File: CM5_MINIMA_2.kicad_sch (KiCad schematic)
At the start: 15 parts, among them J101 USB_C_Receptacle_USB2.0

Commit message: power symbols
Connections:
- net +3V3 renamed +3V3_PI
- no-connect marks 6 -> 7
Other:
- sheet CM5 ports: added none; removed GPIO5, GPIO6, GPIO7
- sheet DSI_CSI ports: added none; removed 3V3
- sheet Ethernet ports: added none; removed 3V3
- sheet HDMI ports: added none; removed 5V
- sheet IO ports: added nLED_ACTIVITY; removed 3V3, 5V, nACTIVITY_LED
- sheet PCIe-M2 ports: added none; removed +5v
- sheet USB ports: added none; removed 5V
- moved on the sheet: C101, C102, TP101

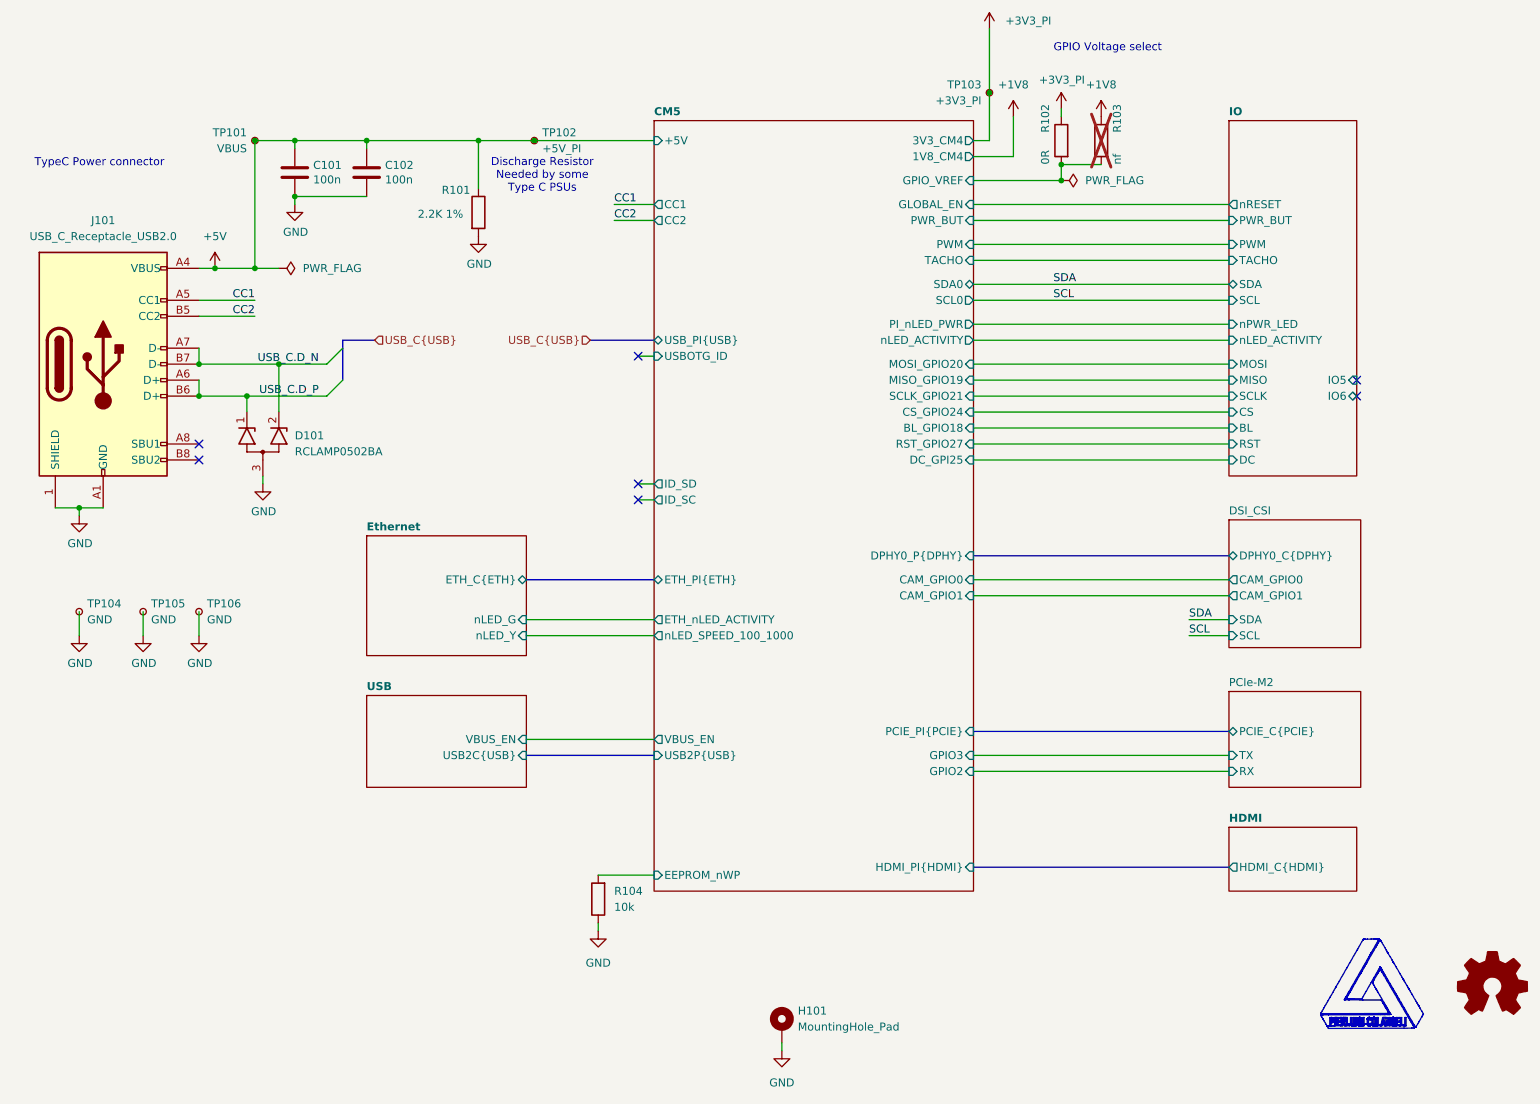
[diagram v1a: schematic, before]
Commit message: changed i2c connector and nrpiboot
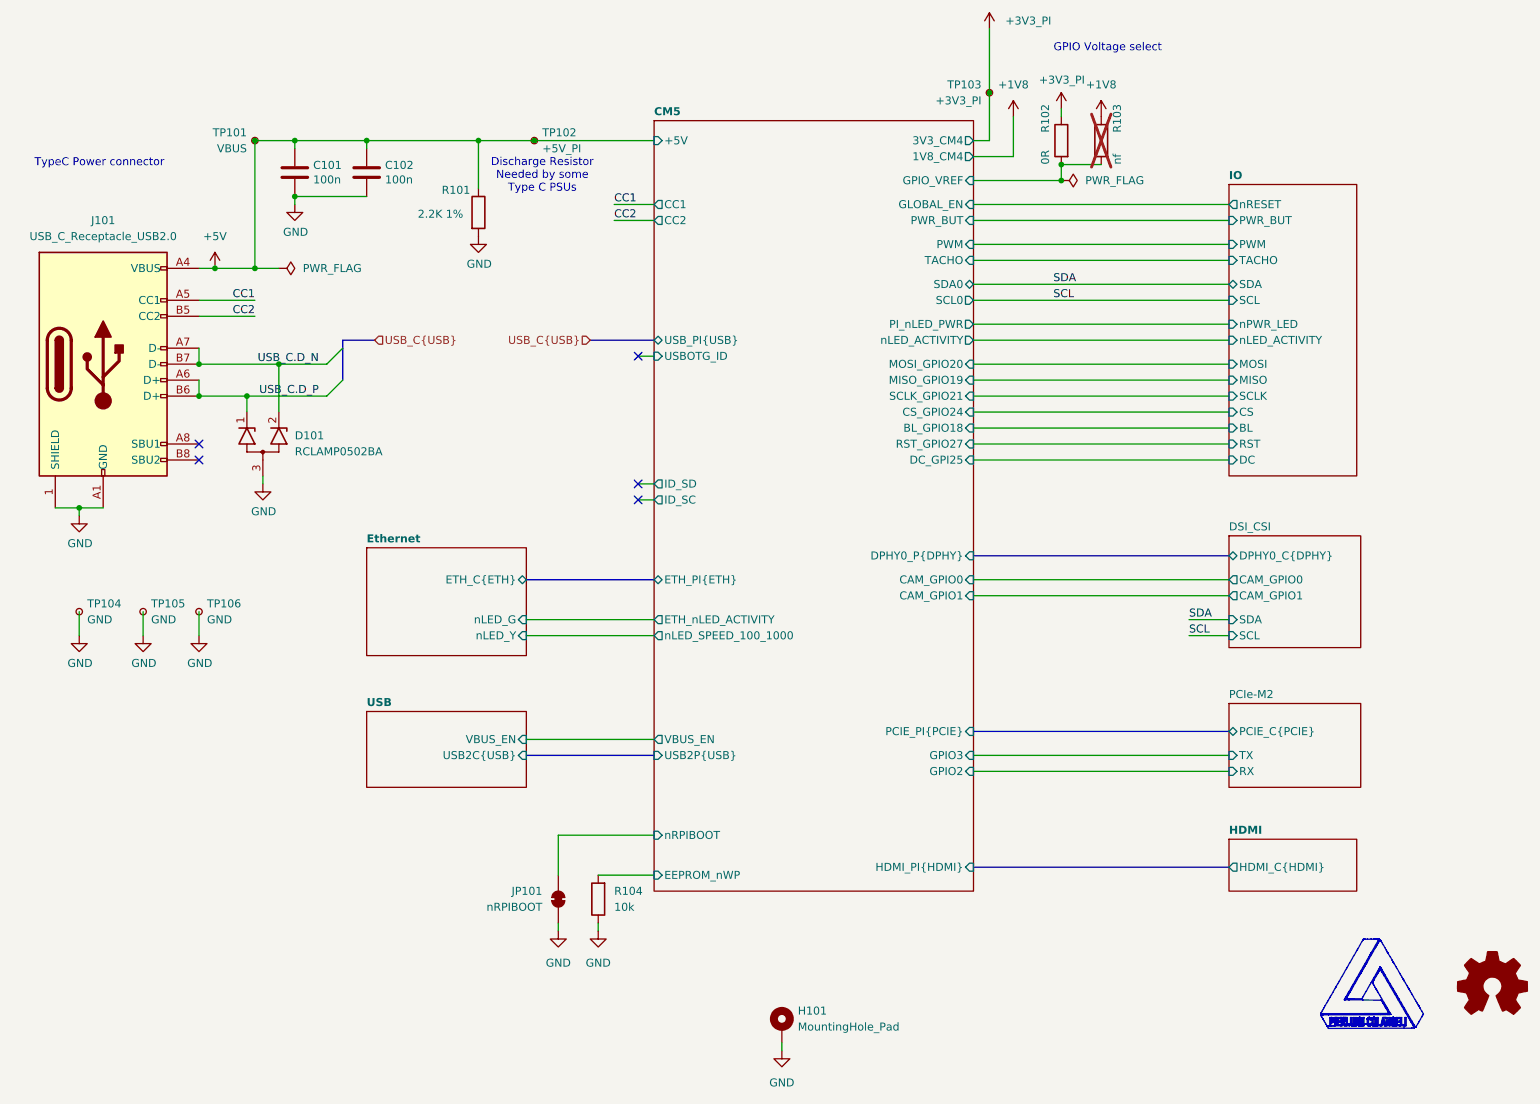
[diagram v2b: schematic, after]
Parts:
- added JP101: nRPIBOOT, Jumper:SolderJumper-2_P1.3mm_Bridged_RoundedPad1.0x1.5mm, symbol Jumper:SolderJumper_2_Bridged
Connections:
- net GND: now also JP101.1 (A)
- new net CM5/nRPIBOOT: JP101.2 (B)
- no-connect marks 7 -> 5
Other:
- sheet CM5 ports: added nRPIBOOT; removed none
- sheet IO ports: added none; removed IO5, IO6
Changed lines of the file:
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@@
 	)
 	(no_connect
-		(at 234.95 80.01)
-	)
-	(no_connect
 		(at 120.65 73.66)
 	)
@@
 		(at 120.65 96.52)
 	)
-	(no_connect
-		(at 234.95 77.47)
-	)
 	(bus_entry
 		(at 71.12 74.93)
@@
 	(wire
 		(pts
+			(xy 107.95 163.83) (xy 107.95 165.1)
+		)
+		(stroke
+			(width 0)
+			(type default)
+		)
+	)
+	(wire
+		(pts
 			(xy 31.75 114.3) (xy 31.75 118.11)
 		)
@@
 		)
 	)
+	(wire
+		(pts
+			(xy 107.95 149.86) (xy 123.19 149.86)
+		)
+		(stroke
+			(width 0)
+			(type default)
+		)
+	)
 	(bus
 		(pts
@@
 	(wire
 		(pts
+			(xy 107.95 149.86) (xy 107.95 156.21)
+		)
+		(stroke
+			(width 0)
+			(type default)
+		)
+	)
+	(wire
+		(pts
 			(xy 77.47 39.37) (xy 95.25 39.37)
 		)
@@
 		)
 	)
+	(symbol
+		(lib_id "Jumper:SolderJumper_2_Bridged")
+		(at 107.95 160.02 270)
+		(mirror x)
+		(unit 1)
+		(exclude_from_sim yes)
+		(in_bom no)
+		(on_board yes)
+		(dnp no)
+		(property "Reference" "JP101"
+			(at 105.41 158.7499 90)
+			(effects
+				(font
+					(size 1.27 1.27)
+				)
+				(justify right)
+			)
+		)
+		(property "Value" "nRPIBOOT"
+			(at 105.41 161.2899 90)
+			(effects
+				(font
+					(size 1.27 1.27)
+				)
+				(justify right)
+			)
+		)
+		(property "Footprint" "Jumper:SolderJumper-2_P1.3mm_Bridged_RoundedPad1.0x1.5mm"
+			(at 107.95 160.02 0)
+			(effects
+				(font
+					(size 1.27 1.27)
+				)
+				(hide yes)
+			)
+		)
+		(property "Datasheet" "~"
+			(at 107.95 160.02 0)
+			(effects
+				(font
+					(size 1.27 1.27)
+				)
+				(hide yes)
+			)
+		)
+		(property "Description" "Solder Jumper, 2-pole, closed/bridged"
+			(at 107.95 160.02 0)
+			(effects
+				(font
+					(size 1.27 1.27)
+				)
+				(hide yes)
+			)
+		)
+		(pin "1"
+		)
+		(pin "2"
+		)
+		(instances
+			(project ""
+				(path "/b33e81d6-18a9-4b9d-a239-76a7c253462f"
+					(reference "JP101")
+					(unit 1)
+				)
+			)
+		)
+	)
+	(symbol
+		(lib_id "power:GND")
+		(at 107.95 165.1 0)
+		(unit 1)
+		(exclude_from_sim no)
+		(in_bom yes)
+		(on_board yes)
+		(dnp no)
+		(fields_autoplaced yes)
+		(property "Reference" "#PWR0105"
+			(at 107.95 171.45 0)
+			(effects
+				(font
+					(size 1.27 1.27)
+				)
+				(hide yes)
+			)
+		)
+		(property "Value" "GND"
+			(at 107.95 170.18 0)
+			(effects
+				(font
+					(size 1.27 1.27)
+				)
+			)
+		)
+		(property "Footprint" ""
+			(at 107.95 165.1 0)
+			(effects
+				(font
+					(size 1.27 1.27)
+				)
+				(hide yes)
+			)
+		)
+		(property "Datasheet" ""
+			(at 107.95 165.1 0)
+			(effects
+				(font
+					(size 1.27 1.27)
+				)
+				(hide yes)
+			)
+		)
+		(property "Description" ""
+			(at 107.95 165.1 0)
+			(effects
+				(font
+					(size 1.27 1.27)
+				)
+				(hide yes)
+			)
+		)
+		(pin "1"
+		)
+		(instances
+			(project "CM5_MINIMA_2"
+				(path "/b33e81d6-18a9-4b9d-a239-76a7c253462f"
+					(reference "#PWR0105")
+					(unit 1)
+				)
+			)
+		)
+	)
 	(sheet
-		(at 77.47 127.635)
-		(size 25.4 14.605)
+		(at 77.47 130.175)
+		(size 25.4 12.065)
 		(fields_autoplaced yes)
 		(stroke
@@
 		)
 		(property "Sheetname" "USB"
-			(at 77.47 126.9234 0)
+			(at 77.47 129.4634 0)
 			(effects
 				(font
@@
 	)
 	(sheet
-		(at 214.63 148.59)
-		(size 20.32 10.16)
+		(at 214.63 150.495)
+		(size 20.32 8.255)
 		(fields_autoplaced yes)
 		(stroke
@@
 		)
 		(property "Sheetname" "HDMI"
-			(at 214.63 147.8784 0)
+			(at 214.63 149.7834 0)
 			(effects
 				(font
@@
 			)
 		)
+		(pin "nRPIBOOT" input
+			(at 123.19 149.86 180)
+			(effects
+				(font
+					(size 1.27 1.27)
+				)
+				(justify left)
+			)
+		)
 		(instances
 			(project "CM5_MINIMA_2"
@@
 	)
 	(sheet
-		(at 214.63 36.195)
-		(size 20.32 56.515)
+		(at 214.63 46.355)
+		(size 20.32 46.355)
 		(fields_autoplaced yes)
 		(stroke
@@
 		)
 		(property "Sheetname" "IO"
-			(at 214.63 35.4834 0)
+			(at 214.63 45.6434 0)
 			(effects
 				(font
@@
 			)
 		)
-		(pin "IO6" bidirectional
-			(at 234.95 80.01 0)
-			(effects
-				(font
-					(size 1.27 1.27)
-				)
-				(justify right)
-			)
-		)
-		(pin "IO5" input
-			(at 234.95 77.47 0)
-			(effects
-				(font
-					(size 1.27 1.27)
-				)
-				(justify right)
-			)
-		)
 		(pin "MOSI" input
 			(at 214.63 74.93 180)
@@
 	)
 	(sheet
-		(at 77.47 102.235)
-		(size 25.4 19.05)
+		(at 77.47 104.14)
+		(size 25.4 17.145)
 		(fields_autoplaced yes)
 		(stroke
@@
 		)
 		(property "Sheetname" "Ethernet"
-			(at 77.47 101.5234 0)
+			(at 77.47 103.4284 0)
 			(effects
 				(font
@@
 	)
 	(sheet
-		(at 214.63 127)
-		(size 20.955 15.24)
+		(at 214.63 128.905)
+		(size 20.955 13.335)
 		(fields_autoplaced yes)
 		(stroke
@@
 		)
 		(property "Sheetname" "PCIe-M2"
-			(at 214.63 126.2884 0)
+			(at 214.63 128.1934 0)
 			(effects
 				(font
@@
 	)
 	(sheet
-		(at 214.63 99.695)
-		(size 20.955 20.32)
+		(at 214.63 102.235)
+		(size 20.955 17.78)
 		(fields_autoplaced yes)
 		(stroke
@@
 		)
 		(property "Sheetname" "DSI_CSI"
-			(at 214.63 98.9834 0)
+			(at 214.63 101.5234 0)
 			(effects
 				(font
